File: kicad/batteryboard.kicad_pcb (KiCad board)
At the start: 2 copper layers, 41.9 x 72.4 mm, 19 parts, among them U1 PANSTAMP_02, U3 DHT22, U4 MAX1724

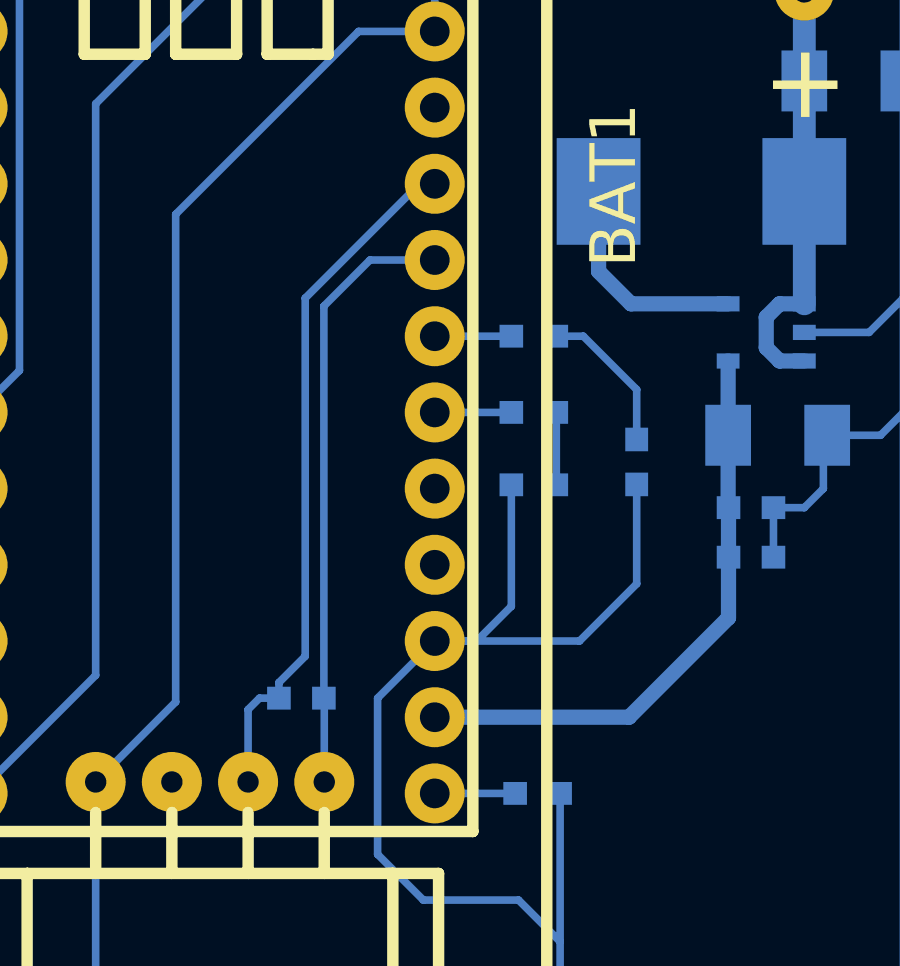
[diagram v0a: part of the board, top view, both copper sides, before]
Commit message: rearrange some modules
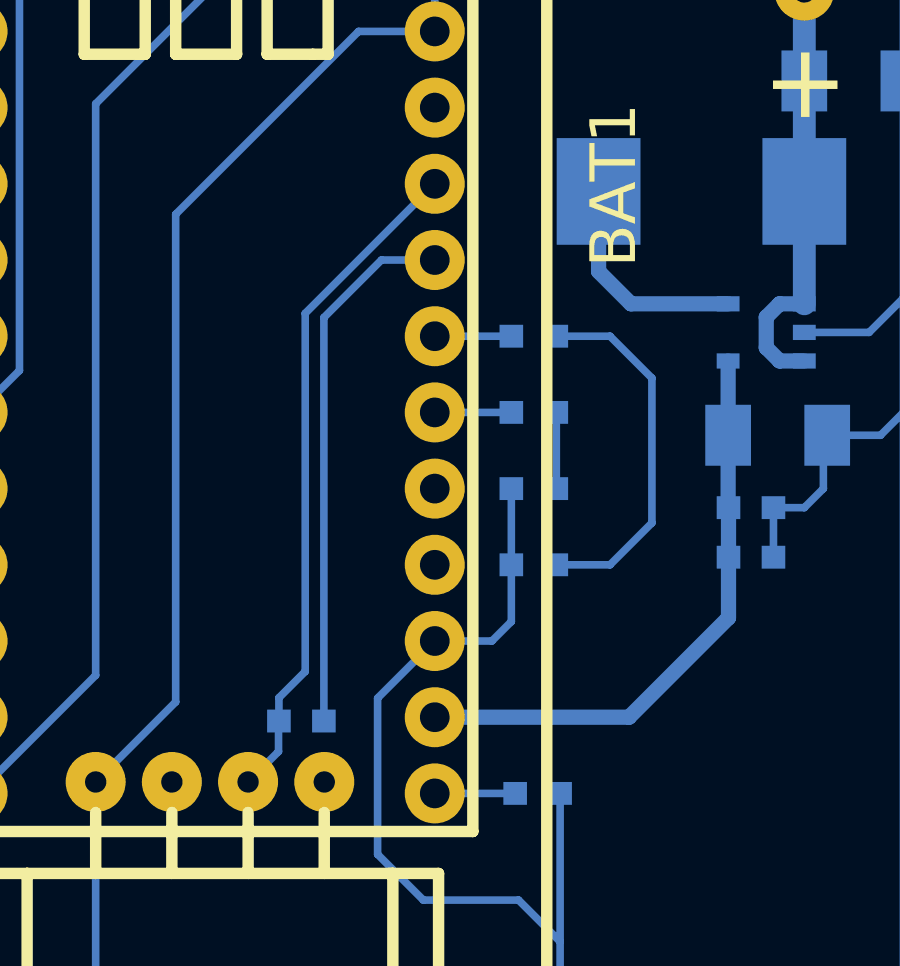
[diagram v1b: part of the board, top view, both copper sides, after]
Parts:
- moved D1 4.85 mm to (182.0, 98.2), turned to 180 degrees
- moved C5 1.65 mm to (189.2, 96.3)
- moved C6 1.65 mm to (189.2, 97.9)
- moved R3 0.76 mm to (174.2, 103.4)
- moved D2 0.13 mm to (182.0, 95.6)
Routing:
- net GND: track 257.1 -> 246.4 mm
- net N-0000023: track 5.08 -> 12.4 mm
- net /A2: track 20.2 -> 17.9 mm
- net /A1: track 23.2 -> 22.5 mm
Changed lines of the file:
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@@
   (general
     (links 33)
-    (no_connects 0)
+    (no_connects 1)
     (area 159.944999 68.504999 202.005001 141.045001)
     (thickness 1.6)
     (drawings 5)
-    (tracks 89)
+    (tracks 86)
     (zones 0)
     (modules 19)
@@
       (drillshape 1)
       (scaleselection 1)
-      (outputdirectory ""))
+      (outputdirectory /tmp/))
   )
   (net 0 "")
@@
   )
   (module SM0603S (layer B.Cu)
-    (at 189.23 96.266)
+    (at 189.23 97.917)
     (attr smd)
     (fp_text reference C6 (at -2.0193 0.03048) (layer B.SilkS)
@@
   )
   (module SM0603S (layer B.Cu)
-    (at 189.23 97.917)
+    (at 189.23 96.266)
     (attr smd)
     (fp_text reference C5 (at -2.0193 0.03048) (layer B.SilkS)
@@
   )
   (module SM0603S (layer B.Cu)
-    (at 174.244 102.616 180)
+    (at 174.244 103.378 180)
     (attr smd)
     (fp_text reference R3 (at -2.0193 0.03048 180) (layer B.SilkS)
@@
   )
   (module SM0603S (layer B.Cu)
-    (at 185.42 94.742 270)
-    (attr smd)
-    (fp_text reference D1 (at -2.0193 0.03048 270) (layer B.SilkS)
-      (effects (font (size 0.635 0.508) (thickness 0.127)) (justify mirror))
-    )
-    (fp_text value LED (at 0.0762 0.0254 270) (layer B.SilkS) hide
+    (at 181.991 98.171 180)
+    (attr smd)
+    (fp_text reference D1 (at -2.0193 0.03048 180) (layer B.SilkS)
+      (effects (font (size 0.635 0.508) (thickness 0.127)) (justify mirror))
+    )
+    (fp_text value LED (at 0.0762 0.0254 180) (layer B.SilkS) hide
       (effects (font (size 0.635 0.508) (thickness 0.127)) (justify mirror))
     )
@@
     (fp_line (start 1.3462 0.5842) (end 1.3462 -0.5842) (layer B.SilkS) (width 0.1524))
     (fp_line (start 1.3462 -0.5842) (end 0.1524 -0.5842) (layer B.SilkS) (width 0.1524))
-    (pad 2 smd rect (at 0.7493 0 270) (size 0.7874 0.762)
-      (layers B.Cu B.Paste B.Mask)
-      (net 8 GND)
-    )
-    (pad 1 smd rect (at -0.7493 0 270) (size 0.7874 0.762)
+    (pad 2 smd rect (at 0.7493 0 180) (size 0.7874 0.762)
+      (layers B.Cu B.Paste B.Mask)
+      (net 8 GND)
+    )
+    (pad 1 smd rect (at -0.7493 0 180) (size 0.7874 0.762)
       (layers B.Cu B.Paste B.Mask)
       (net 10 N-0000023)
@@
   )
   (module SM0603S (layer B.Cu)
-    (at 181.991 95.504 180)
+    (at 181.991 95.631 180)
     (attr smd)
     (fp_text reference D2 (at -2.0193 0.03048 180) (layer B.SilkS)
@@
   (segment (start 188.468 96.2533) (end 188.4807 96.266) (width 0.508) (layer B.Cu) (net 1))
   (segment (start 188.468 91.3765) (end 188.468 93.853) (width 0.508) (layer B.Cu) (net 1))
-  (segment (start 173.4947 102.616) (end 173.4947 102.0953) (width 0.254) (layer B.Cu) (net 2))
-  (segment (start 178.181 85.471) (end 178.689 85.471) (width 0.254) (layer B.Cu) (net 2))
-  (segment (start 174.371 89.281) (end 178.181 85.471) (width 0.254) (layer B.Cu) (net 2))
-  (segment (start 174.371 101.219) (end 174.371 89.281) (width 0.254) (layer B.Cu) (net 2))
-  (segment (start 173.4947 102.0953) (end 174.371 101.219) (width 0.254) (layer B.Cu) (net 2))
-  (segment (start 172.466 105.41) (end 172.466 102.997) (width 0.254) (layer B.Cu) (net 2))
-  (segment (start 172.847 102.616) (end 173.4947 102.616) (width 0.254) (layer B.Cu) (net 2))
-  (segment (start 172.466 102.997) (end 172.847 102.616) (width 0.254) (layer B.Cu) (net 2))
-  (segment (start 174.9933 102.616) (end 174.9933 89.5477) (width 0.254) (layer B.Cu) (net 3))
-  (segment (start 176.53 88.011) (end 178.689 88.011) (width 0.254) (layer B.Cu) (net 3))
-  (segment (start 174.9933 89.5477) (end 176.53 88.011) (width 0.254) (layer B.Cu) (net 3))
-  (segment (start 175.006 105.41) (end 175.006 102.6287) (width 0.254) (layer B.Cu) (net 3))
-  (segment (start 175.006 102.6287) (end 174.9933 102.616) (width 0.254) (layer B.Cu) (net 3))
-  (segment (start 191.008 79.02956) (end 183.80456 79.02956) (width 0.254) (layer B.Cu) (net 4) (status 400000))
-  (segment (start 167.386 101.854) (end 163.449 105.791) (width 0.254) (layer B.Cu) (net 4) (status 800000))
+  (segment (start 173.4947 103.378) (end 173.4947 102.6033) (width 0.254) (layer B.Cu) (net 2) (status 400000))
+  (segment (start 174.371 89.789) (end 178.689 85.471) (width 0.254) (layer B.Cu) (net 2) (status 800000))
+  (segment (start 174.371 101.727) (end 174.371 89.789) (width 0.254) (layer B.Cu) (net 2))
+  (segment (start 173.4947 102.6033) (end 174.371 101.727) (width 0.254) (layer B.Cu) (net 2))
+  (segment (start 172.466 105.41) (end 173.482 104.394) (width 0.254) (layer B.Cu) (net 2) (status 400000))
+  (segment (start 173.482 103.3907) (end 173.4947 103.378) (width 0.254) (layer B.Cu) (net 2) (status C00000))
+  (segment (start 173.482 104.394) (end 173.482 103.3907) (width 0.254) (layer B.Cu) (net 2) (status 800000))
+  (segment (start 174.9933 103.378) (end 174.9933 89.9287) (width 0.254) (layer B.Cu) (net 3) (status 400000))
+  (segment (start 176.911 88.011) (end 178.689 88.011) (width 0.254) (layer B.Cu) (net 3) (status 800000))
+  (segment (start 174.9933 89.9287) (end 176.911 88.011) (width 0.254) (layer B.Cu) (net 3))
+  (segment (start 191.008 79.02956) (end 183.80456 79.02956) (width 0.254) (layer B.Cu) (net 4))
+  (segment (start 167.386 101.854) (end 163.449 105.791) (width 0.254) (layer B.Cu) (net 4))
   (segment (start 167.386 82.804) (end 167.386 101.854) (width 0.254) (layer B.Cu) (net 4))
   (segment (start 173.863 76.327) (end 167.386 82.804) (width 0.254) (layer B.Cu) (net 4))
@@
   (segment (start 181.2417 90.551) (end 178.689 90.551) (width 0.254) (layer B.Cu) (net 6))
   (segment (start 181.3687 105.791) (end 178.689 105.791) (width 0.254) (layer B.Cu) (net 7))
-  (segment (start 163.449 77.851) (end 171.45 77.851) (width 0.254) (layer B.Cu) (net 8) (status 400000))
-  (segment (start 194.31 78.994) (end 194.31 82.042) (width 0.254) (layer B.Cu) (net 8) (status 800000))
+  (segment (start 181.2417 98.171) (end 181.2417 100.0633) (width 0.254) (layer B.Cu) (net 8))
+  (segment (start 180.594 100.711) (end 178.689 100.711) (width 0.254) (layer B.Cu) (net 8))
+  (segment (start 181.2417 100.0633) (end 180.594 100.711) (width 0.254) (layer B.Cu) (net 8))
+  (segment (start 181.2417 95.631) (end 181.2417 98.171) (width 0.254) (layer B.Cu) (net 8))
+  (segment (start 163.449 77.851) (end 171.45 77.851) (width 0.254) (layer B.Cu) (net 8))
+  (segment (start 194.31 78.994) (end 194.31 82.042) (width 0.254) (layer B.Cu) (net 8))
   (segment (start 191.008 75.692) (end 194.31 78.994) (width 0.254) (layer B.Cu) (net 8))
   (segment (start 173.609 75.692) (end 191.008 75.692) (width 0.254) (layer B.Cu) (net 8))
@@
   (segment (start 167.386 121.539) (end 176.87544 131.02844) (width 0.254) (layer B.Cu) (net 8))
   (segment (start 176.87544 131.02844) (end 191.008 131.02844) (width 0.254) (layer B.Cu) (net 8))
-  (segment (start 185.42 95.4913) (end 185.42 98.806) (width 0.254) (layer B.Cu) (net 8))
-  (segment (start 183.515 100.711) (end 178.689 100.711) (width 0.254) (layer B.Cu) (net 8))
-  (segment (start 185.42 98.806) (end 183.515 100.711) (width 0.254) (layer B.Cu) (net 8))
   (segment (start 178.689 100.711) (end 176.784 102.616) (width 0.254) (layer B.Cu) (net 8))
+  (segment (start 176.784 102.616) (end 176.784 107.823) (width 0.254) (layer B.Cu) (net 8))
+  (segment (start 176.784 107.823) (end 178.308 109.347) (width 0.254) (layer B.Cu) (net 8))
+  (segment (start 178.308 109.347) (end 181.483 109.347) (width 0.254) (layer B.Cu) (net 8))
   (segment (start 181.483 109.347) (end 182.8673 110.7313) (width 0.254) (layer B.Cu) (net 8))
-  (segment (start 178.308 109.347) (end 181.483 109.347) (width 0.254) (layer B.Cu) (net 8))
-  (segment (start 176.784 107.823) (end 178.308 109.347) (width 0.254) (layer B.Cu) (net 8))
-  (segment (start 176.784 102.616) (end 176.784 107.823) (width 0.254) (layer B.Cu) (net 8))
   (segment (start 182.8673 105.791) (end 182.8673 110.7313) (width 0.254) (layer B.Cu) (net 8))
   (segment (start 182.8673 110.7313) (end 182.8673 126.2253) (width 0.254) (layer B.Cu) (net 8))
   (segment (start 182.8673 126.2253) (end 187.67044 131.02844) (width 0.254) (layer B.Cu) (net 8))
   (segment (start 187.67044 131.02844) (end 191.008 131.02844) (width 0.254) (layer B.Cu) (net 8))
-  (segment (start 181.2417 95.504) (end 181.2417 99.5553) (width 0.254) (layer B.Cu) (net 8))
-  (segment (start 181.2417 99.5553) (end 180.086 100.711) (width 0.254) (layer B.Cu) (net 8))
-  (segment (start 180.086 100.711) (end 178.689 100.711) (width 0.254) (layer B.Cu) (net 8))
   (segment (start 191.008 90.424) (end 193.167 90.424) (width 0.254) (layer B.Cu) (net 8))
   (segment (start 193.167 90.424) (end 194.31 89.281) (width 0.254) (layer B.Cu) (net 8))
@@
   (segment (start 189.9793 96.266) (end 189.9793 97.917) (width 0.254) (layer B.Cu) (net 8))
   (segment (start 178.689 77.851) (end 178.689 80.391) (width 0.254) (layer B.Cu) (net 8))
-  (segment (start 182.7403 93.091) (end 182.7403 95.504) (width 0.254) (layer B.Cu) (net 9))
-  (segment (start 185.42 93.9927) (end 185.42 92.329) (width 0.254) (layer B.Cu) (net 10))
-  (segment (start 183.642 90.551) (end 182.7403 90.551) (width 0.254) (layer B.Cu) (net 10))
-  (segment (start 185.42 92.329) (end 183.642 90.551) (width 0.254) (layer B.Cu) (net 10))
+  (segment (start 182.7403 95.631) (end 182.7403 93.091) (width 0.254) (layer B.Cu) (net 9))
+  (segment (start 182.7403 90.551) (end 184.531 90.551) (width 0.254) (layer B.Cu) (net 10))
+  (segment (start 184.531 98.171) (end 182.7403 98.171) (width 0.254) (layer B.Cu) (net 10))
+  (segment (start 185.928 96.774) (end 184.531 98.171) (width 0.254) (layer B.Cu) (net 10))
+  (segment (start 185.928 91.948) (end 185.928 96.774) (width 0.254) (layer B.Cu) (net 10))
+  (segment (start 184.531 90.551) (end 185.928 91.948) (width 0.254) (layer B.Cu) (net 10))
   (segment (start 184.15 85.725) (end 184.15 88.392) (width 0.508) (layer B.Cu) (net 11))
   (segment (start 185.2295 89.4715) (end 188.468 89.4715) (width 0.508) (layer B.Cu) (net 11))

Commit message: update version number
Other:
- board text added: "pantempi v1.0"
- board text removed: "pantempi v0.2b"
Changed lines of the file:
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@@
     )
   )
-  (gr_text "pantempi\nv0.2b" (at 180.721 71.12) (layer B.Cu)
+  (gr_text "pantempi\nv1.0" (at 180.721 71.12) (layer B.Cu)
     (effects (font (size 1.5 1.5) (thickness 0.3)) (justify mirror))
   )

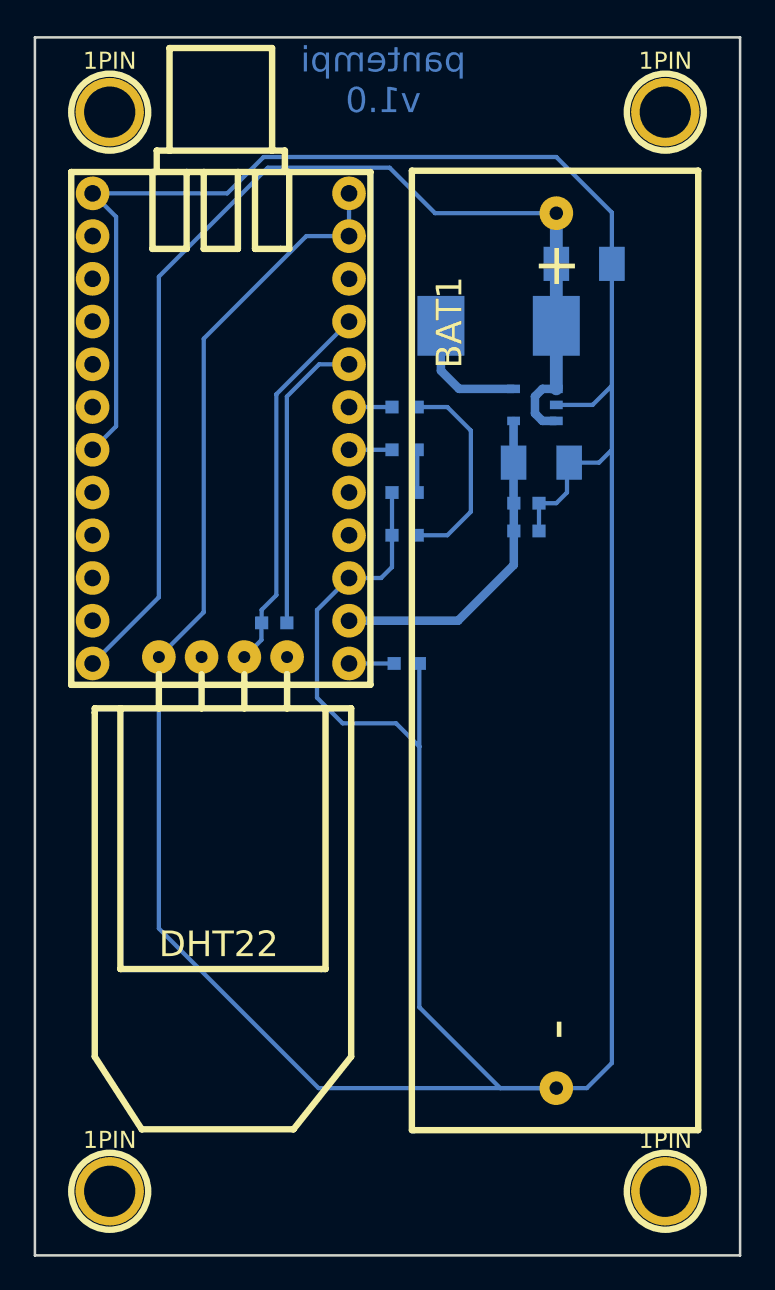
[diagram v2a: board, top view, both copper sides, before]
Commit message: Update kicad files for pantempi v1.1
Committing these as obtained from Peter.
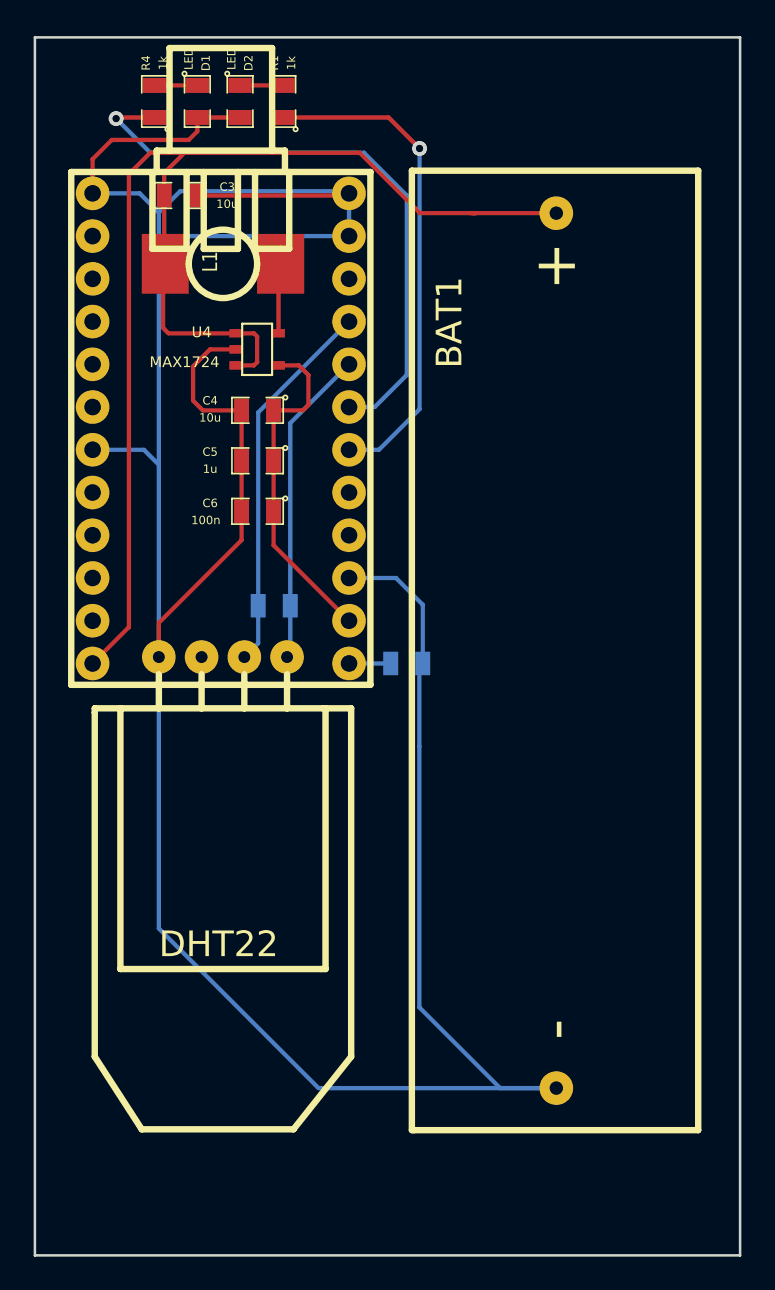
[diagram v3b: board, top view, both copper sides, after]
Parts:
- removed 1PIN (x4): P***, 1pin
- C3, C4: footprint SM1206 -> SM0805; moved to F.Cu
- C5, C6, D1, D2, R1, R4: footprint SM0603S -> SM0805; moved to F.Cu
- L1, U4: moved to F.Cu
- R2, R3: footprint SM0603S -> SM0805
- moved D1 28.6 mm to (169.7, 72.4), turned to 270 degrees
- moved D2 25.2 mm to (172.2, 72.4), turned to 270 degrees
- moved C3 24.3 mm to (168.7, 78.0)
- moved R4 23.5 mm to (167.1, 72.4), turned to 90 degrees
- moved R1 21.9 mm to (174.8, 72.4), turned to 90 degrees
- moved C4 17.1 mm to (173.3, 90.7), turned to 180 degrees
- moved U4 16.8 mm to (173.2, 87.1)
- moved L1 16.8 mm to (171.2, 82.0)
- moved C5 16.2 mm to (173.3, 93.7), turned to 180 degrees
- moved C6 16.0 mm to (173.3, 96.7), turned to 180 degrees
- moved R3 1.02 mm to (174.2, 102.4)
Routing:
- net GND: track 246.4 -> 191.4 mm
- net /LED2: track 2.55 -> 36.4 mm, vias 0 -> 1
- net /LED1: track 2.55 -> 29.6 mm, vias 0 -> 1
- net /BATTERY: track 66.4 -> 78.0 mm
- net N-0000023: track 12.4 -> 2.54 mm
- net N-0000024: track 7.43 -> 4.18 mm
- net /A2: track 17.9 -> 18.9 mm
- net +3.3V: track 19.7 -> 20.4 mm
- added copper zone on F.Cu, net GND
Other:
- board text added: "pantempi v1.1"
- board text removed: "pantempi v1.0"
